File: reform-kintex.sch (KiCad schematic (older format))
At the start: 4 parts, among them J1 Conn_01x33, U1 MNT Reform 2.0 SoM Socket

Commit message: some work on 6 power supplies, SPI flash
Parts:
- U1: symbol reform2-som:reform2-som-connector -> reform-kintex-rescue:reform2-som-connector-reform2-som
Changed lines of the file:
@@
 	5750 2450 6650 2450
 $Comp
-L reform2-som:reform2-som-connector U1
+L reform-kintex-rescue:reform2-som-connector-reform2-som U1
 U 1 1 60678A3C
 P 4850 7250

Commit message: fully routed
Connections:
- net GND: no longer U1.13 (GND), U1.25 (GND)
- no-connect marks 75 -> 77
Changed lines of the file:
@@
 	1    0    0    -1
 $EndComp
-Connection ~ 3100 3050
-Wire Wire Line
-	3100 2750 3100 3050
 Wire Wire Line
 	4050 2750 3100 2750
 Connection ~ 3100 3350
 Wire Wire Line
-	3100 3050 3100 3350
-Wire Wire Line
-	4050 3050 3100 3050
-Connection ~ 3100 3650
-Wire Wire Line
-	3100 3350 3100 3650
-Wire Wire Line
 	4050 3350 3100 3350
 Connection ~ 3100 3950
-Wire Wire Line
-	3100 3650 3100 3950
-Wire Wire Line
-	4050 3650 3100 3650
 Connection ~ 3100 4450
 Wire Wire Line
@@
 F1 "RAM.sch" 50
 $EndSheet
+Wire Wire Line
+	3100 2750 3100 3350
+NoConn ~ 4050 3050
+Wire Wire Line
+	3100 3350 3100 3950
+NoConn ~ 4050 3650
 $EndSCHEMATC

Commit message: connect some missing i2c signals, backlight_en
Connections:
- net GND: no longer U1.104 (GND)
- no-connect marks 77 -> 78
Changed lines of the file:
@@
 Wire Wire Line
 	5750 7050 6650 7050
-Connection ~ 6650 7550
-Wire Wire Line
-	6650 7250 6650 7550
 Wire Wire Line
 	5750 7250 6650 7250
 Connection ~ 6650 7850
-Wire Wire Line
-	6650 7550 6650 7850
-Wire Wire Line
-	5750 7550 6650 7550
 Connection ~ 6650 8150
 Wire Wire Line
@@
 	3100 3350 3100 3950
 NoConn ~ 4050 3650
+Wire Wire Line
+	6650 7250 6650 7850
+NoConn ~ 5750 7550
 $EndSCHEMATC

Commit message: silkscreen cleanup, 3d models, some footprint fixes
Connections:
- net EDP_SCL renamed DISP1_SCL
- net EDP_SDA renamed DISP1_SDA
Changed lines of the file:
@@
 USB2_TX_N
 Text GLabel 4000 7850 0    50   BiDi ~ 0
-EDP_SDA
+DISP1_SDA
 Text GLabel 4000 7750 0    50   Input ~ 0
-EDP_SCL
+DISP1_SCL
 Text GLabel 5800 5350 2    50   Input ~ 0
 PCIE1_CLK_N

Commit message: DRC, polishing, bugfixes, badge
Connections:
- net BOOTCFG_10: no longer names the net of U1.134 (SAI1_TXD2)
- net BOOTCFG_12: no longer names the net of U1.138 (SAI1_TXD4)
- net BOOTCFG_13: no longer names the net of U1.140 (SAI1_TXD5)
- net BOOTCFG_4: no longer names the net of U1.152 (SAI1_RXD4)
- net EDP_IRQ: no longer names the net of U1.40 (WL_IRQ)
- net ETH0_LED_LINK2: no longer names the net of U1.81 (JTAG_NTRST)
- net JTAG_TCK: no longer names the net of U1.73 (JTAG_TCK)
- net JTAG_TDI: no longer names the net of U1.75 (JTAG_TDI)
- net JTAG_TMS: no longer names the net of U1.77 (JTAG_TMS)
- net LPC_MISO: no longer names the net of U1.93 (ECSPI2_MISO)
- net LPC_MOSI: no longer names the net of U1.91 (ECSPI2_MOSI)
- net LPC_SCK: no longer names the net of U1.97 (ECSPI2_SCLK)
- net LPC_SS0: no longer names the net of U1.89 (ECSPI2_SS0)
- net MB_SWITCH_1: no longer names the net of U1.139 (FAST_BOOT)
- net RTC_IRQ: no longer names the net of U1.141 (RTC_IRQ)
- net SOC_WAKE: no longer names the net of U1.145 (GPIO1_IO3)
- net TESTPOINT_1: no longer names the net of U1.35 (USB1_OTG_ID)
- net TESTPOINT_2: no longer names the net of U1.8 (PMIC_ON_REQ)
- net TESTPOINT_3: no longer names the net of U1.174 (SAI2_RXC)
- net TESTPOINT_5: no longer names the net of U1.143 (GP_M4_NMI)
- net TESTPOINT_PWM_4: no longer names the net of U1.180 (SAI3_MCLK/PWM4)
- net USB_PWR: no longer names the net of U1.118 (USB1_VBUS)
- no-connect marks 78 -> 100
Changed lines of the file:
@@
 Text GLabel 5800 4250 2    50   Input ~ 0
 EDP_RESETn
-Text GLabel 5800 4350 2    50   Output ~ 0
-EDP_IRQ
-Text GLabel 4000 6150 0    50   Output ~ 0
-JTAG_TDI
 NoConn ~ 5750 4150
 NoConn ~ 5750 4050
@@
 Text GLabel 5800 3850 2    50   Input ~ 0
 UART3_TX
-Text GLabel 4000 6850 0    50   Input ~ 0
-LPC_SS0
 NoConn ~ 5750 8350
 Text GLabel 4000 4250 0    50   Input ~ 0
 PCIE1_RESETn
-Wire Wire Line
-	2850 6450 4050 6450
-Connection ~ 2850 6450
-Wire Wire Line
-	2850 6250 2850 6450
-Wire Wire Line
-	2750 6250 2850 6250
-Wire Wire Line
-	2850 6550 2750 6550
-Connection ~ 2850 6550
-Wire Wire Line
-	2850 6650 2850 6550
-Wire Wire Line
-	2750 6650 2850 6650
-Wire Wire Line
-	2750 6450 2850 6450
-Wire Wire Line
-	4050 6550 2850 6550
 NoConn ~ 5750 4450
 NoConn ~ 5750 3750
@@
 	1    0    0    -1
 $EndComp
-Text GLabel 4000 7250 0    50   Input ~ 0
-LPC_SCK
-Text GLabel 4000 6950 0    50   Input ~ 0
-LPC_MOSI
-Text GLabel 4000 7050 0    50   Output ~ 0
-LPC_MISO
-Text GLabel 2750 6250 0    60   Input ~ 0
-ETH0_LED_LINK2
 Text GLabel 5800 8450 2    50   Output ~ 0
 UART2_RX
@@
 Wire Wire Line
 	2750 6350 4050 6350
-Text GLabel 5800 8250 2    50   Output ~ 0
-USB_PWR
 Wire Wire Line
 	6650 1800 6650 2450
@@
 Text GLabel 4000 6750 0    50   Output ~ 0
 SOC_RESETn
-Text GLabel 2750 6450 0    50   Output ~ 0
-JTAG_RSTn
-Text GLabel 4000 6050 0    50   Output ~ 0
-JTAG_TCK
-Text GLabel 4000 6250 0    50   Output ~ 0
-JTAG_TMS
-Text GLabel 2750 6650 0    50   Input ~ 0
-JTAG_TDO
 Text GLabel 4000 7450 0    50   Input ~ 0
 DAC_SCL
@@
 Wire Wire Line
 	5750 10550 5800 10550
-Wire Wire Line
-	4050 9650 4000 9650
-Text GLabel 4000 9650 0    50   Output ~ 0
-SOC_WAKE
 $Comp
 L power:+5V #PWR0104
@@
 Text Notes 6750 5650 0    50   ~ 0
 PCIe slot 2 reference clock coming\nfrom motherboard synthesizer
-Text GLabel 5800 11350 2    50   Input ~ 0
-TESTPOINT_PWM_4
 Text GLabel 5800 3550 2    50   Input ~ 0
 PCIE2_RESETn
-Wire Wire Line
-	5800 9950 5750 9950
-Text GLabel 5800 9050 2    50   Input ~ 0
-BOOTCFG_10
-Wire Wire Line
-	5800 9050 5750 9050
-Wire Wire Line
-	5800 9250 5750 9250
-Text GLabel 5800 9350 2    50   Input ~ 0
-BOOTCFG_13
-Wire Wire Line
-	5800 9350 5750 9350
-Text GLabel 5800 9250 2    50   Input ~ 0
-BOOTCFG_12
 Text GLabel 9200 3950 2    50   Input ~ 0
 DSI_CLK_N
@@
 Text GLabel 9200 3350 2    50   Input ~ 0
 DSI_D0_N
-Text GLabel 5800 9950 2    50   Input ~ 0
-BOOTCFG_4
-Text GLabel 4000 9450 0    50   Output ~ 0
-RTC_IRQ
-Wire Wire Line
-	4050 9450 4000 9450
 Wire Wire Line
 	4000 4250 4050 4250
-Wire Wire Line
-	5800 11350 5750 11350
 Wire Wire Line
 	5800 11150 5750 11150
@@
 NoConn ~ 5750 11650
 NoConn ~ 4050 4350
-Text GLabel 4000 4150 0    50   BiDi ~ 0
-TESTPOINT_1
-Text GLabel 5800 2750 2    50   BiDi ~ 0
-TESTPOINT_2
 Text Notes 6750 5350 0    50   ~ 0
 PCIe slot 1 reference clock coming\nfrom this module
-Text GLabel 5800 11050 2    50   BiDi ~ 0
-TESTPOINT_3
-Wire Wire Line
-	5800 11050 5750 11050
-Text GLabel 4000 9550 0    50   Output ~ 0
-TESTPOINT_5
-Wire Wire Line
-	4050 9550 4000 9550
-Text GLabel 4000 9350 0    50   Output ~ 0
-MB_SWITCH_1
-Wire Wire Line
-	4000 9350 4050 9350
 Wire Wire Line
 	4000 10550 4050 10550
@@
 Text Notes 1900 6550 2    50   ~ 0
 ETH LEDs\n(JTAG optional on MB)
-Wire Wire Line
-	4000 4150 4050 4150
 Text GLabel 4000 3150 0    60   Input ~ 0
 ETH0_C-
@@
 	4000 3850 4050 3850
 Wire Wire Line
-	4000 6050 4050 6050
-Wire Wire Line
-	4050 6150 4000 6150
-Wire Wire Line
-	4000 6250 4050 6250
-Wire Wire Line
 	4000 6750 4050 6750
 Wire Wire Line
-	4050 6850 4000 6850
-Wire Wire Line
-	4000 6950 4050 6950
-Wire Wire Line
-	4050 7050 4000 7050
-Wire Wire Line
-	4000 7250 4050 7250
-Wire Wire Line
 	4000 7650 4050 7650
 Wire Wire Line
@@
 	5750 8750 5800 8750
 Wire Wire Line
-	5800 8250 5750 8250
-Wire Wire Line
-	5750 2750 5800 2750
-Wire Wire Line
 	5800 2950 5750 2950
 Wire Wire Line
@@
 Wire Wire Line
 	5800 4250 5750 4250
-Wire Wire Line
-	5750 4350 5800 4350
 Wire Wire Line
 	5800 4650 5750 4650
@@
 	6650 7250 6650 7850
 NoConn ~ 5750 7550
+NoConn ~ 4050 6450
+NoConn ~ 4050 6050
+NoConn ~ 4050 6150
+NoConn ~ 4050 6250
+Wire Wire Line
+	2750 6550 4050 6550
+NoConn ~ 4050 6850
+NoConn ~ 4050 6950
+NoConn ~ 4050 7050
+NoConn ~ 4050 7250
+NoConn ~ 5750 2750
+NoConn ~ 5750 4350
+NoConn ~ 5750 8250
+NoConn ~ 5750 9950
+NoConn ~ 5750 9050
+NoConn ~ 5750 9250
+NoConn ~ 5750 9350
+NoConn ~ 5750 11050
+NoConn ~ 5750 11350
+NoConn ~ 4050 4150
+NoConn ~ 4050 9350
+NoConn ~ 4050 9450
+NoConn ~ 4050 9550
+NoConn ~ 4050 9650
 $EndSCHEMATC

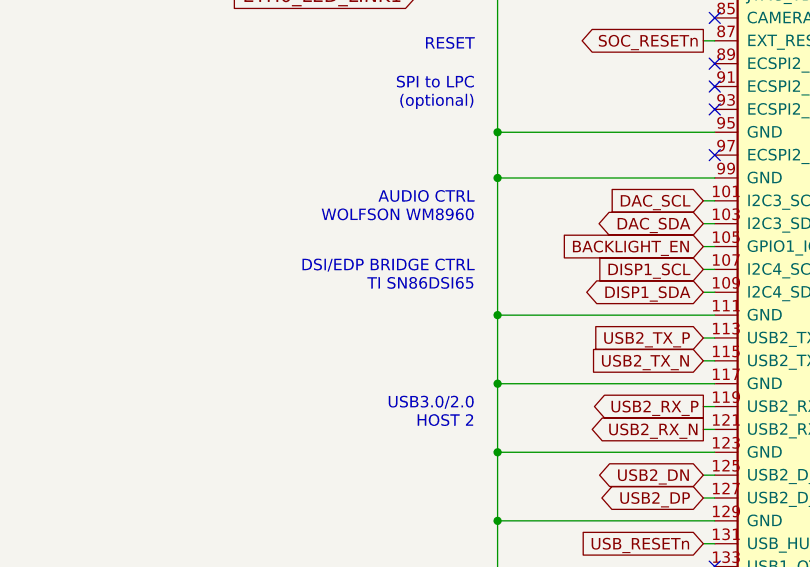
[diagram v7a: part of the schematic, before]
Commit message: add some notes, gerbes and BOM after first D-1 bringup
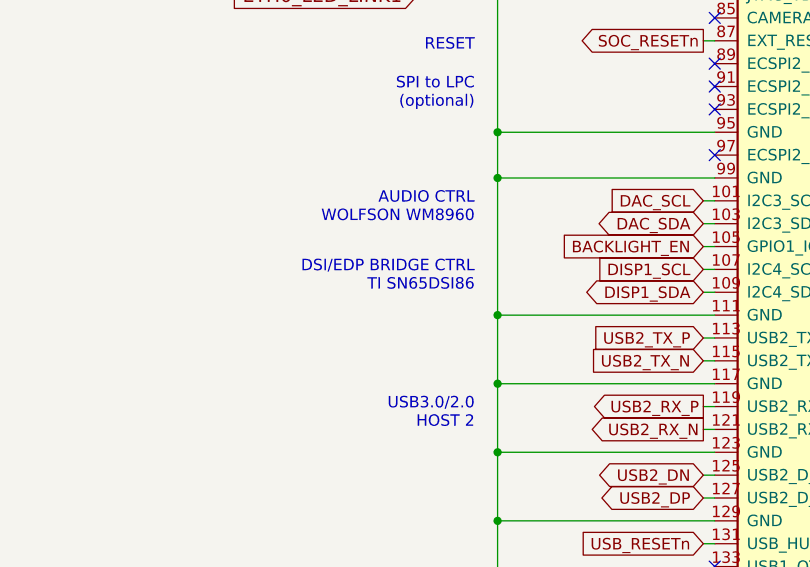
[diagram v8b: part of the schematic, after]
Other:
- note added: "DSI/EDP BRIDGE CTRL\nTI SN65DSI86"
- note removed: "DSI/EDP BRIDGE CTRL\nTI SN86DSI65"
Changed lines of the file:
@@
 AUDIO CTRL\nWOLFSON WM8960
 Text Notes 3000 7850 2    50   ~ 0
-DSI/EDP BRIDGE CTRL\nTI SN86DSI65
+DSI/EDP BRIDGE CTRL\nTI SN65DSI86
 Text Notes 6750 3950 0    50   ~ 0
 UART (optional) to \nSystem Controller (LPC)
